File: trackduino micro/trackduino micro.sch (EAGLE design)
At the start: 27 parts, among them IC2 74AHC1G125DBV, SW1 SPST_TACT-KMR2, U1 ATMEGA168, Y1 16MHZ

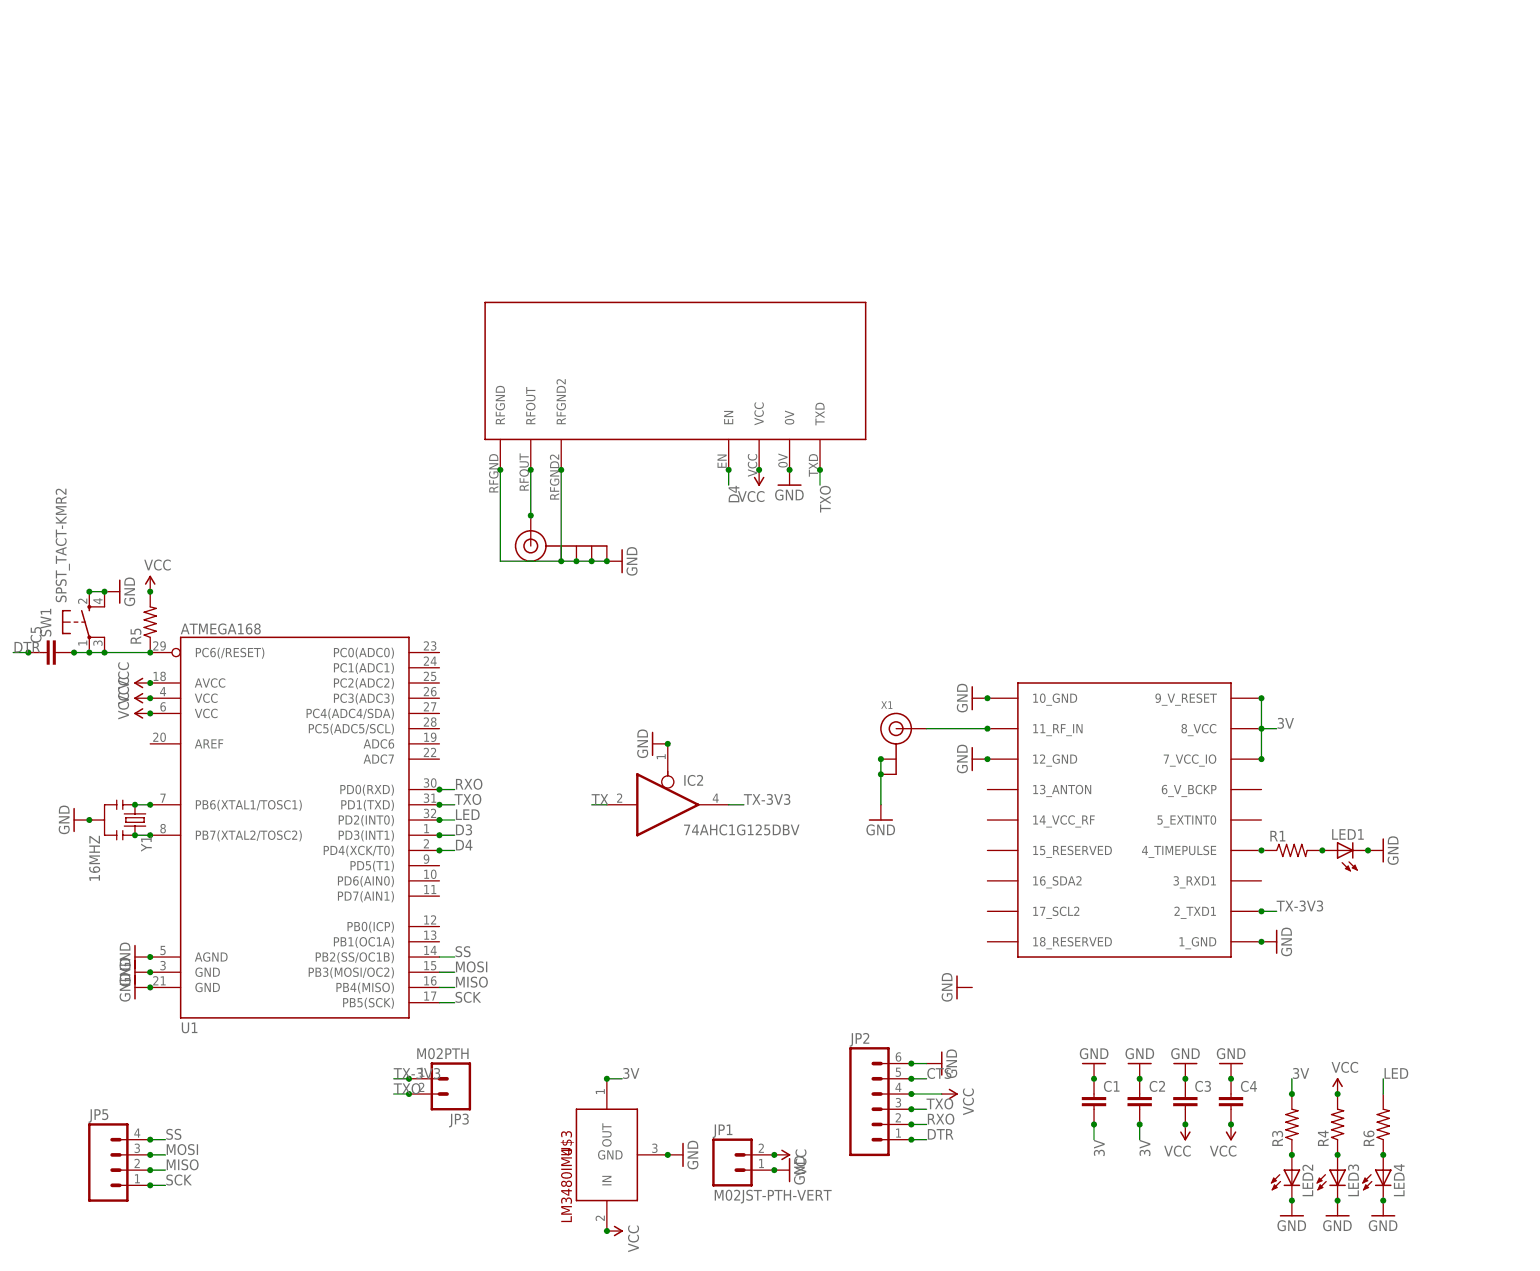
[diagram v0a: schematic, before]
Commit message: removed level shifters
removed unnecessary 5v level shifters from boards.
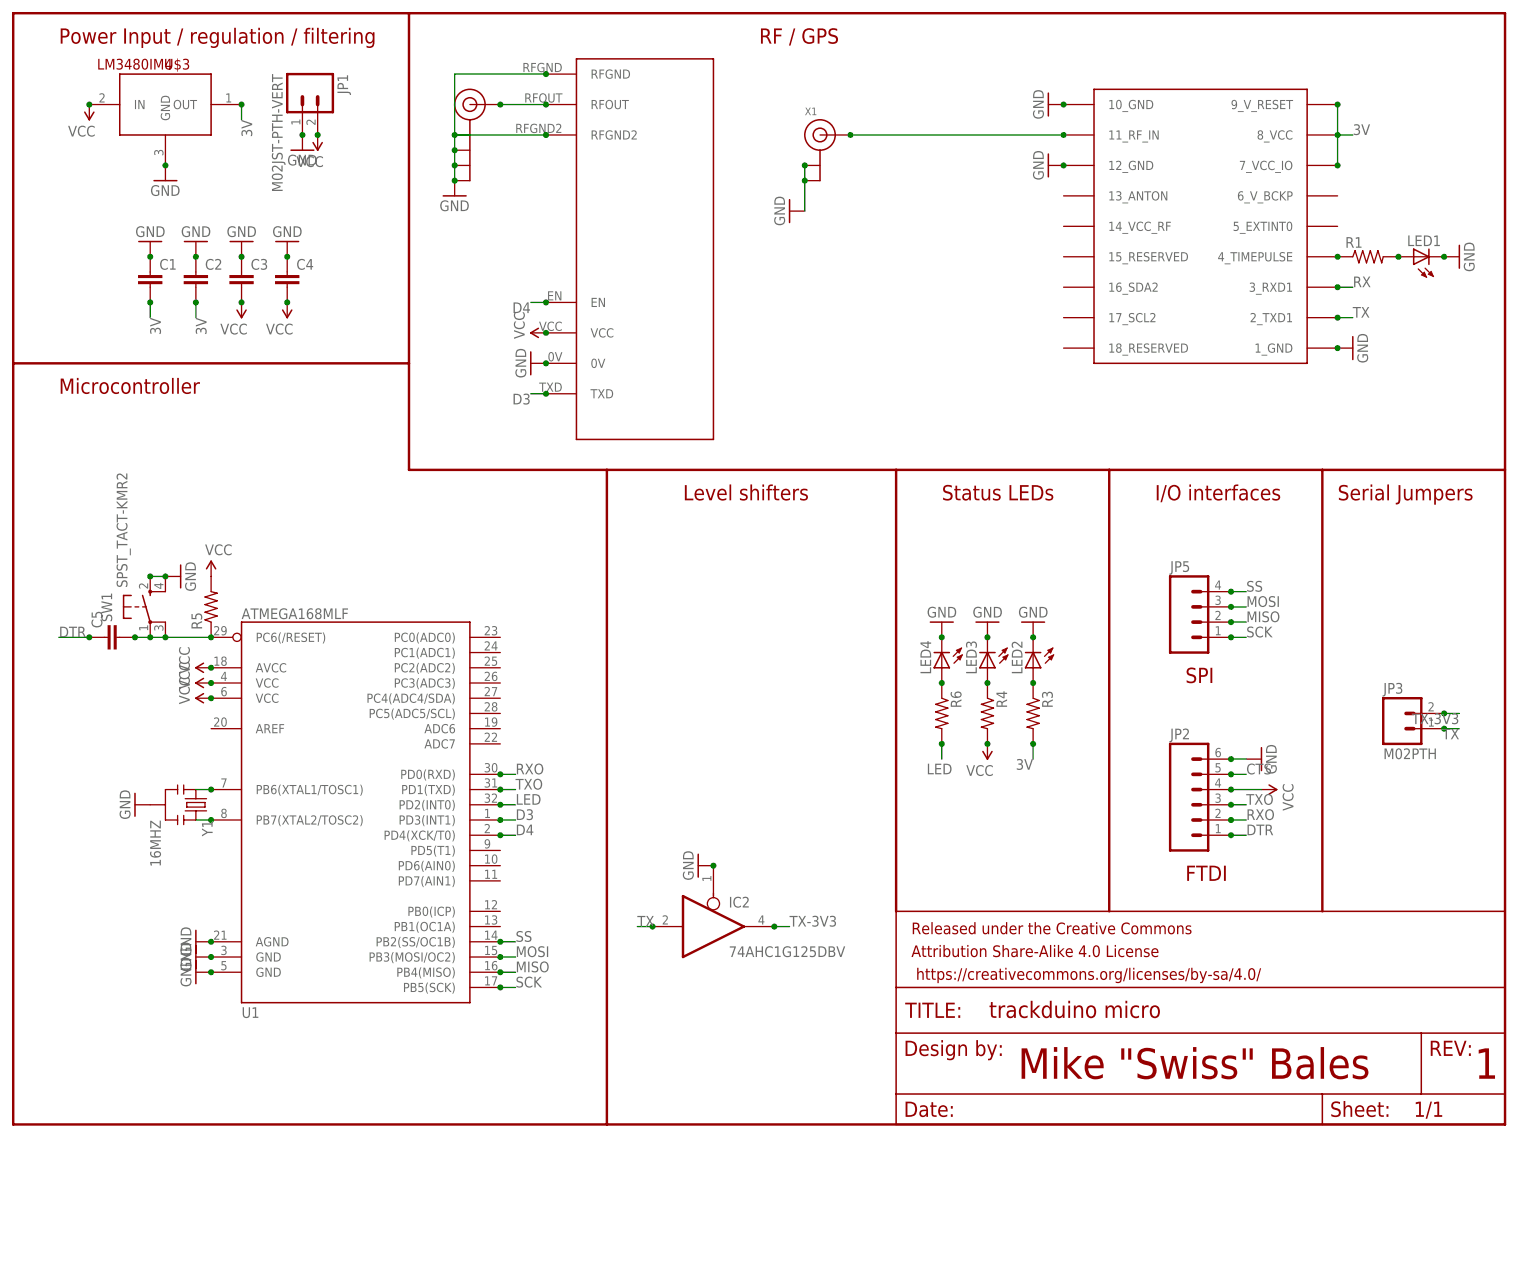
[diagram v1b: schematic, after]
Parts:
- added FRAME1: FRAME-LETTER, SparkFun-Aesthetics:FRAME-LETTER
- U1: value ATMEGA168 -> ATMEGA168MLF; device SparkFun-DigitalIC:ATMEGA168 -> SparkFun-DigitalIC:ATMEGA168MLF
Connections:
- new net RX: U$1.3_RXD1
- net D3: now also U$2.TXD
- net TX: now also JP3.1, U$1.2_TXD1
- net TX-3V3: now also JP3.2; no longer JP3.1, U$1.2_TXD1
- net TXO: no longer JP3.2, U$2.TXD
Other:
- note added: "1"
- note added: "FTDI"
- note added: "I/O interfaces"
- note added: "Level shifters"
- note added: "Microcontroller"
- note added: "Mike "Swiss" Bales"
- note added: "Power Input / regulation / filtering"
- note added: "RF / GPS"
- note added: "SPI"
- note added: "Serial Jumpers"
- note added: "Status LEDs"
- moved on the sheet: C1, C2, C3, C4, C5, IC2, JP1, JP2, JP3, JP5, LED1, LED2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

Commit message: re-routed micro board
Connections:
- net RXO: now also IC2A.I
- net TX: no longer IC2A.I
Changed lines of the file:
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@@
 <net name="TX" class="0">
-<segment>
-<pinref part="IC2" gate="A" pin="I"/>
-<wire x1="106.68" y1="33.02" x2="104.14" y2="33.02" width="0.1524" layer="91"/>
-<label x="104.14" y="33.02" size="1.778" layer="95"/>
-<junction x="106.68" y="33.02"/>
-</segment>
 <segment>
 <wire x1="220.98" y1="134.62" x2="223.52" y2="134.62" width="0.1524" layer="91"/>
@@
 <junction x="203.2" y="50.8"/>
 </segment>
-</net>
+<segment>
+<pinref part="IC2" gate="A" pin="I"/>
+<wire x1="106.68" y1="33.02" x2="104.14" y2="33.02" width="0.1524" layer="91"/>
+<label x="104.14" y="33.02" size="1.778" layer="95"/>
+<junction x="106.68" y="33.02"/>
+</segment>
+</net>

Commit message: minor fixes
boards ordered.
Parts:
- U1: value ATMEGA168MLF -> ATMEGA168; device SparkFun-DigitalIC:ATMEGA168MLF -> SparkFun-DigitalIC:ATMEGA168
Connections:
- net TX: no longer U$1.2_TXD1
- net TX-3V3: now also U$1.2_TXD1
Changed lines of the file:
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@@
 <parts>
 <part name="IC2" library="74xx-little-us" deviceset="74*1G125" device="DBV" technology="AHC"/>
-<part name="U1" library="SparkFun-DigitalIC" deviceset="ATMEGA168" device="MLF" value="ATMEGA168MLF"/>
+<part name="U1" library="SparkFun-DigitalIC" deviceset="ATMEGA168" device="" value="ATMEGA168"/>
 <part name="U$2" library="Ava" deviceset="RADIOMETRIX-HX1" device=""/>
 <part name="U$3" library="SparkFun-PowerIC" deviceset="LM3480IM4" device=""/>
@@
 <junction x="238.76" y="68.58"/>
 </segment>
+<segment>
+<wire x1="220.98" y1="134.62" x2="223.52" y2="134.62" width="0.1524" layer="91"/>
+<label x="223.52" y="134.62" size="1.778" layer="95"/>
+<pinref part="U$1" gate="G$1" pin="2_TXD1"/>
+<junction x="220.98" y="134.62"/>
+</segment>
 </net>
 <net name="D3" class="0">
@@
 <net name="TX" class="0">
 <segment>
-<wire x1="220.98" y1="134.62" x2="223.52" y2="134.62" width="0.1524" layer="91"/>
-<label x="223.52" y="134.62" size="1.778" layer="95"/>
-<pinref part="U$1" gate="G$1" pin="2_TXD1"/>
-<junction x="220.98" y="134.62"/>
-</segment>
-<segment>
 <pinref part="JP3" gate="G$1" pin="1"/>
